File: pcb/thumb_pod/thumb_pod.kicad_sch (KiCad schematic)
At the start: 41 parts, among them J1 Conn_02x06_Odd_Even, J2 Conn_02x06_Odd_Even, J3 Conn_02x06_Odd_Even, SW1 SW_Push, SW10 SW_Push, SW2 SW_Push, SW3 SW_Push, SW4 SW_Push, SW5 SW_Push, SW6 SW_Push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

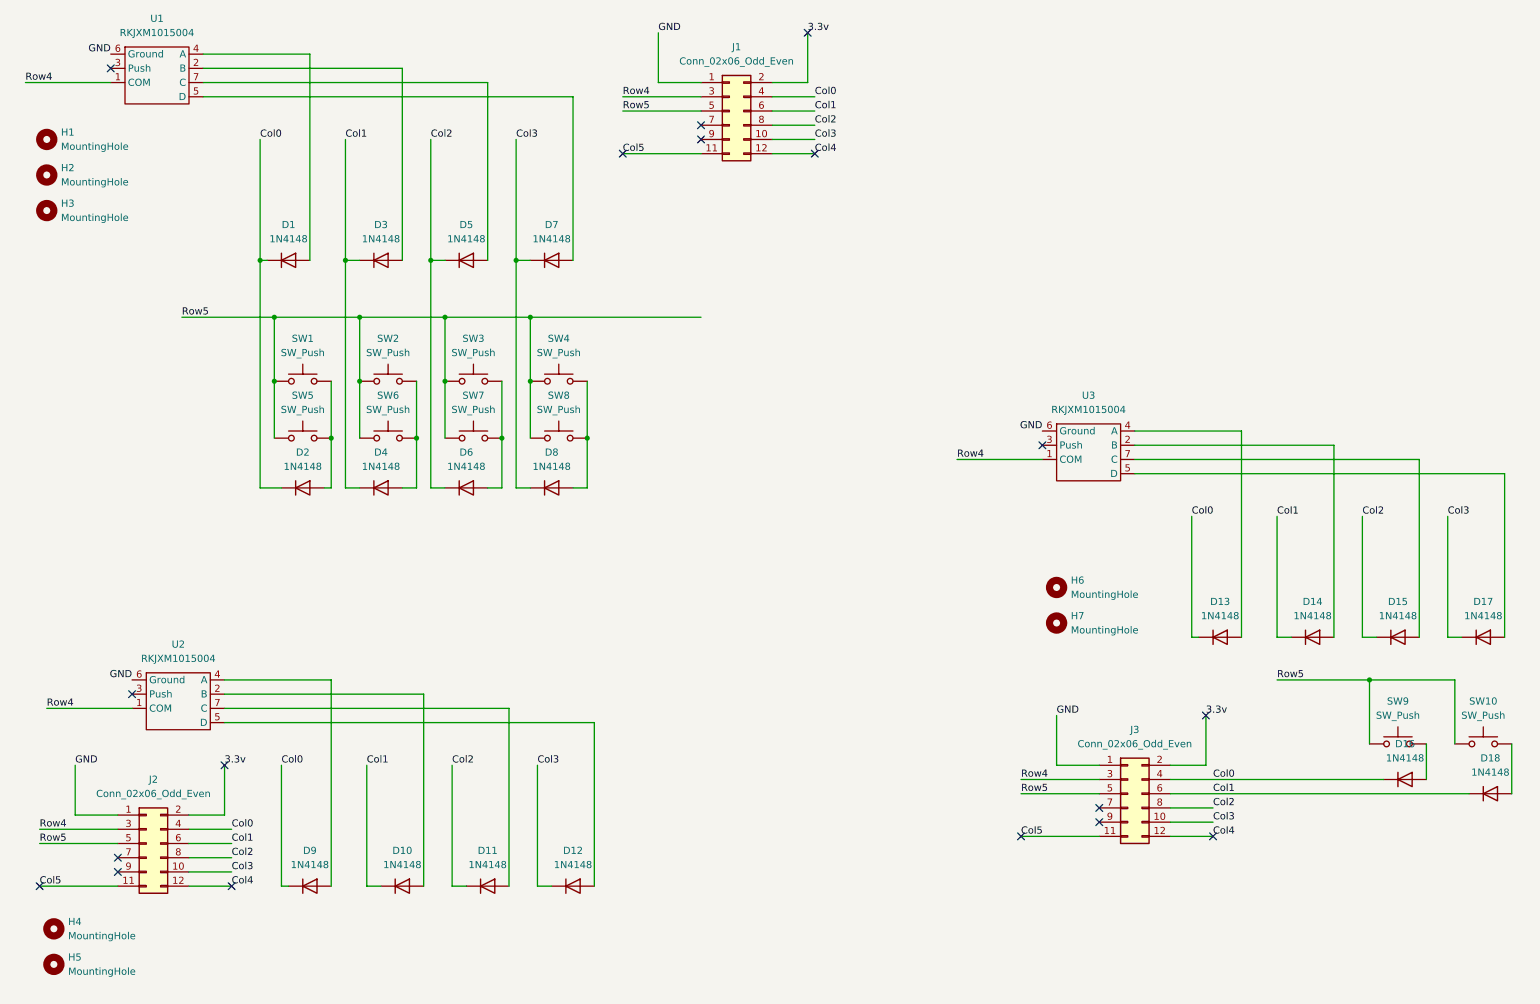
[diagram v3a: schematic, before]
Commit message: - Rearranged sub-boards to (hopefully) make manufacturing easier  - Fixed the schematic to better isolate each thumb pod version
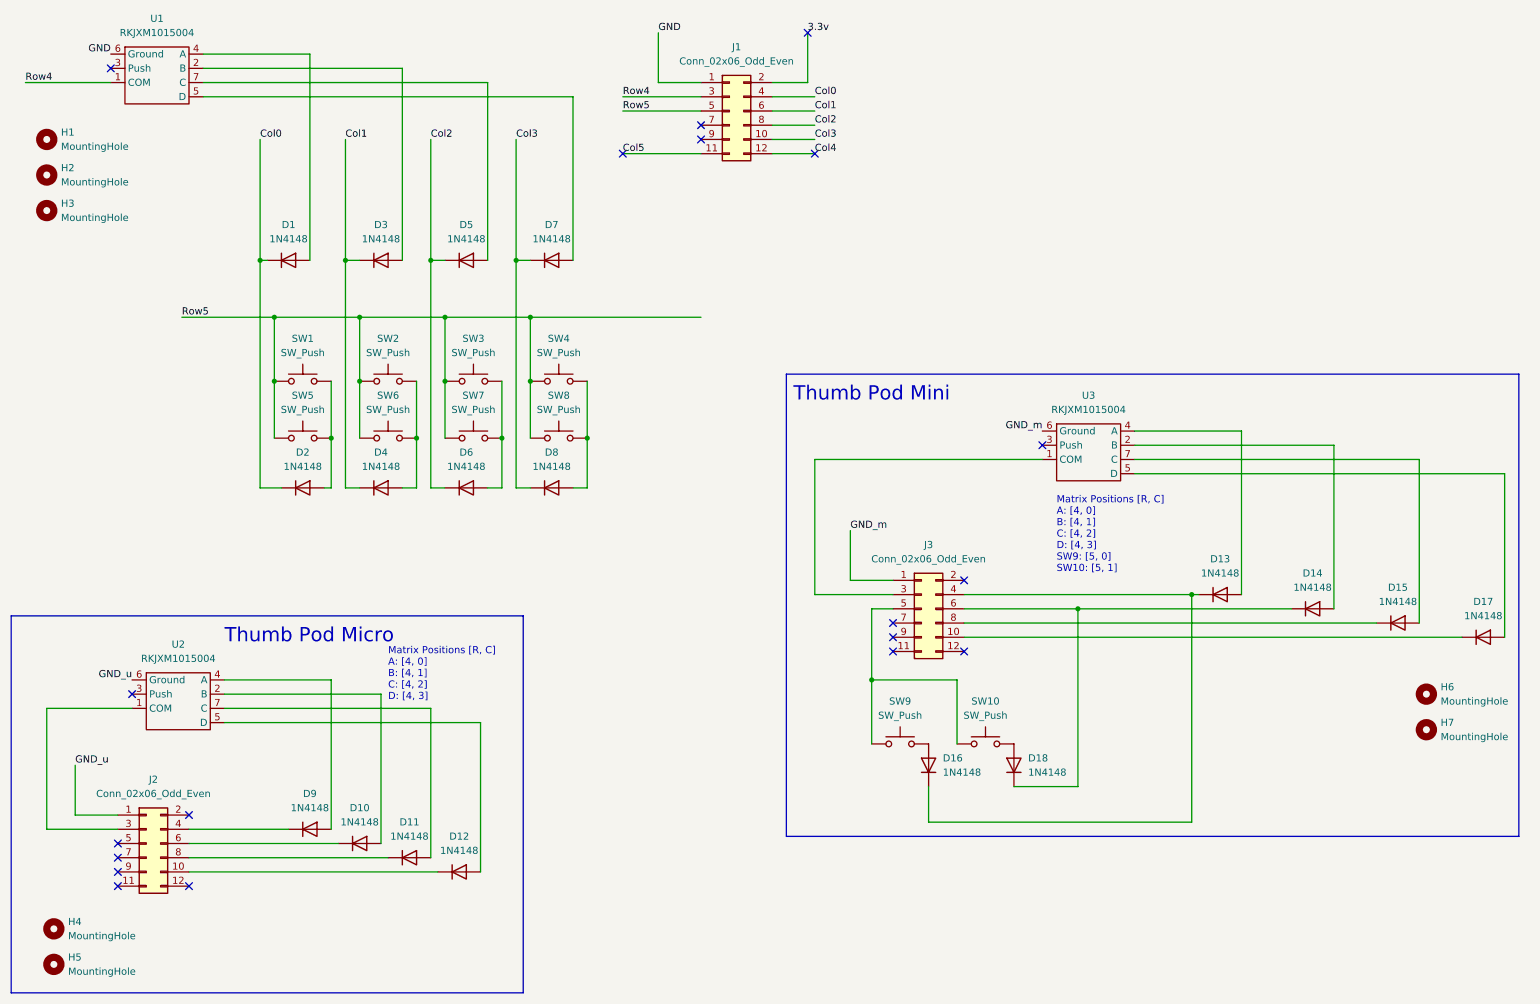
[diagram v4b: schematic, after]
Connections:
- net 3.3v: no longer J2.2 (Pin_2), J3.2 (Pin_2)
- net Col0: no longer D13.1 (K), D16.1 (K), D9.1 (K), J2.4 (Pin_4), J3.4 (Pin_4)
- net Col1: no longer D10.1 (K), D14.1 (K), D18.1 (K), J2.6 (Pin_6), J3.6 (Pin_6)
- net Col2: no longer D11.1 (K), D15.1 (K), J2.8 (Pin_8), J3.8 (Pin_8)
- net Col3: no longer D12.1 (K), D17.1 (K), J2.10 (Pin_10), J3.10 (Pin_10)
- net Col4: no longer J2.12 (Pin_12), J3.12 (Pin_12)
- net Col5: no longer J2.11 (Pin_11), J3.11 (Pin_11)
- net GND: no longer J2.1 (Pin_1), J3.1 (Pin_1), U2.6 (Ground), U3.6 (Ground)
- net Row4: no longer J2.3 (Pin_3), J3.3 (Pin_3), U2.1 (COM), U3.1 (COM)
- net Row5: no longer J2.5 (Pin_5), J3.5 (Pin_5), SW10.1, SW9.1
- new net: D14.1 (K), D18.1 (K), J3.6 (Pin_6)
- new net: D9.1 (K), J2.4 (Pin_4)
- new net: D13.1 (K), D16.1 (K), J3.4 (Pin_4)
- new net: D10.1 (K), J2.6 (Pin_6)
- new net: D11.1 (K), J2.8 (Pin_8)
- new net: D12.1 (K), J2.10 (Pin_10)
- new net: J2.3 (Pin_3), U2.1 (COM)
- new net: J3.5 (Pin_5), SW10.1, SW9.1
- new net: J3.3 (Pin_3), U3.1 (COM)
- new net: D17.1 (K), J3.10 (Pin_10)
- new net: D15.1 (K), J3.8 (Pin_8)
- new net GND_m: J3.1 (Pin_1), U3.6 (Ground)
- new net GND_u: J2.1 (Pin_1), U2.6 (Ground)
- no-connect marks 18 -> 19
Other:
- note added: "Matrix Positions [R, C] A: [4, 0] B: [4, 1] C: [4, 2] D: [4, 3]"
- note added: "Matrix Positions [R, C] A: [4, 0] B: [4, 1] C: [4, 2] D: [4, 3] SW9: [5, 0] SW10: [5, 1]"
- note added: "Thumb Pod Micro"
- note added: "Thumb Pod Mini"
- moved on the sheet: D10, D11, D12, D13, D14, D15, D16, D18, D9, H6, H7, J3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
